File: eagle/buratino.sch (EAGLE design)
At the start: 50 parts, among them IC1 LTC3105MS, J2 AVR_SPI, J4 Ext Battery, Q2 2n7002PW, U4 ATMEGA256RFR2, U7 SWITCH, U8 LED-RGB, X1 16MHz, X2 32.768k, Y1 ANTENNA2SMD5

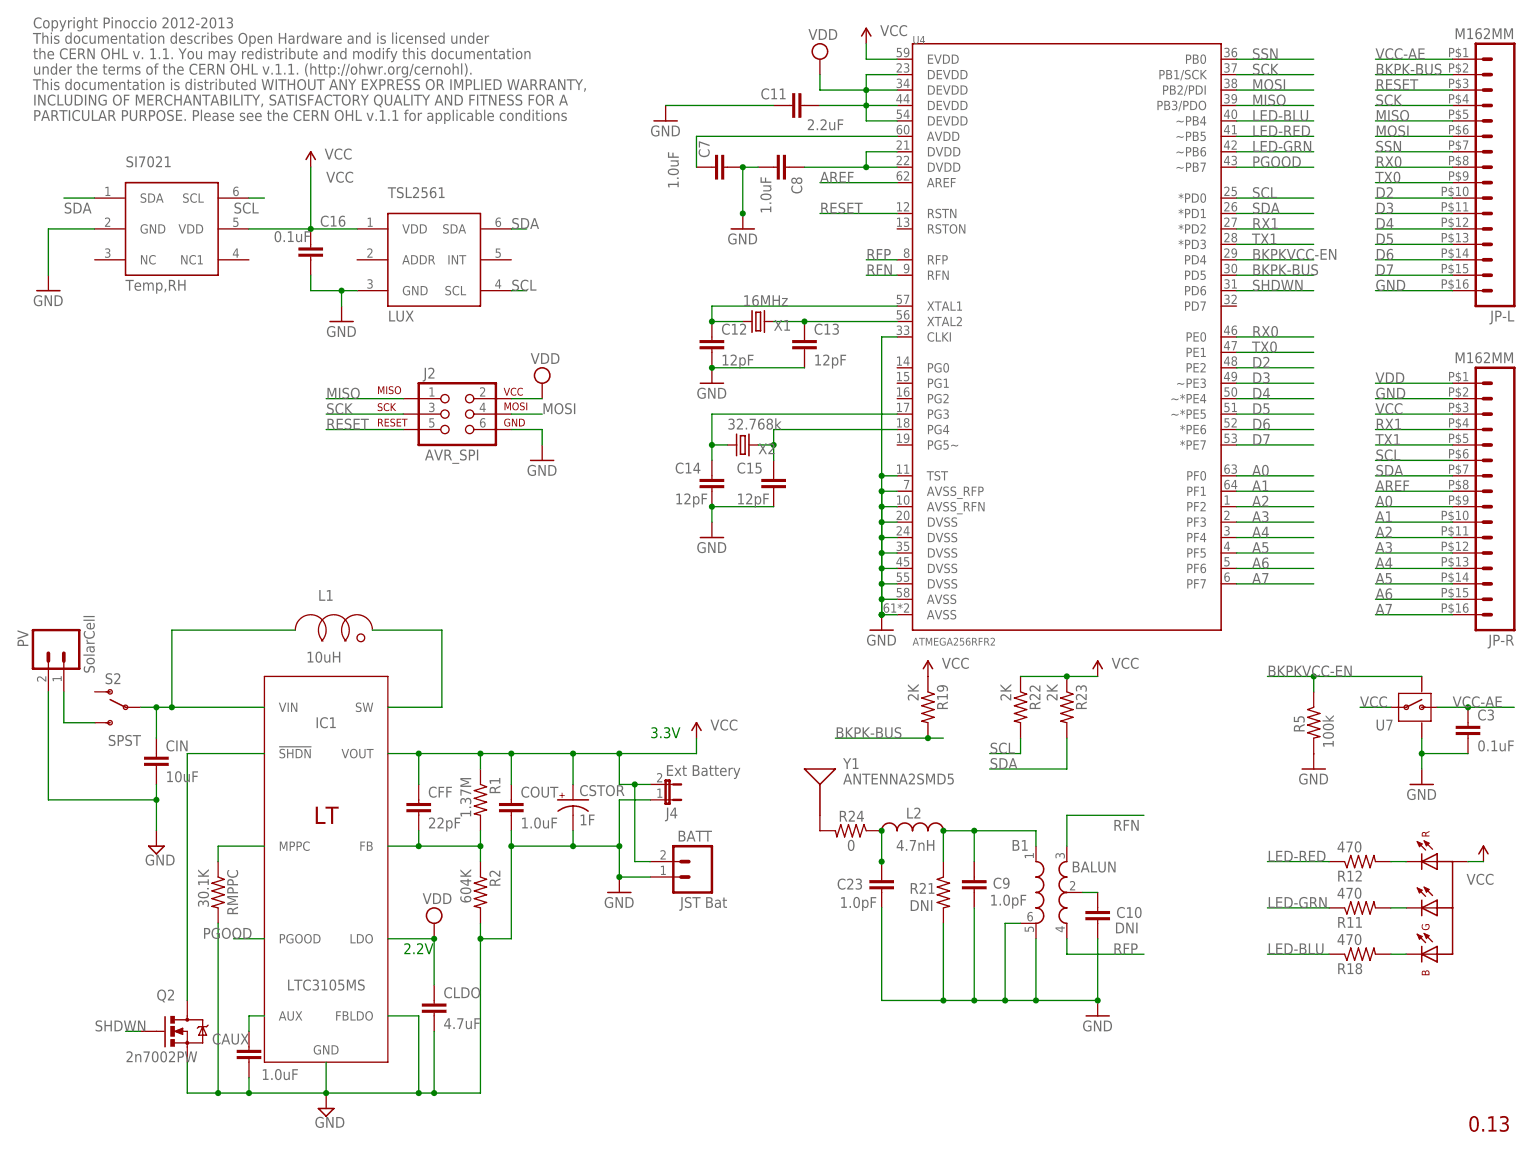
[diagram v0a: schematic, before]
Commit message: replace ICSP with JTAG
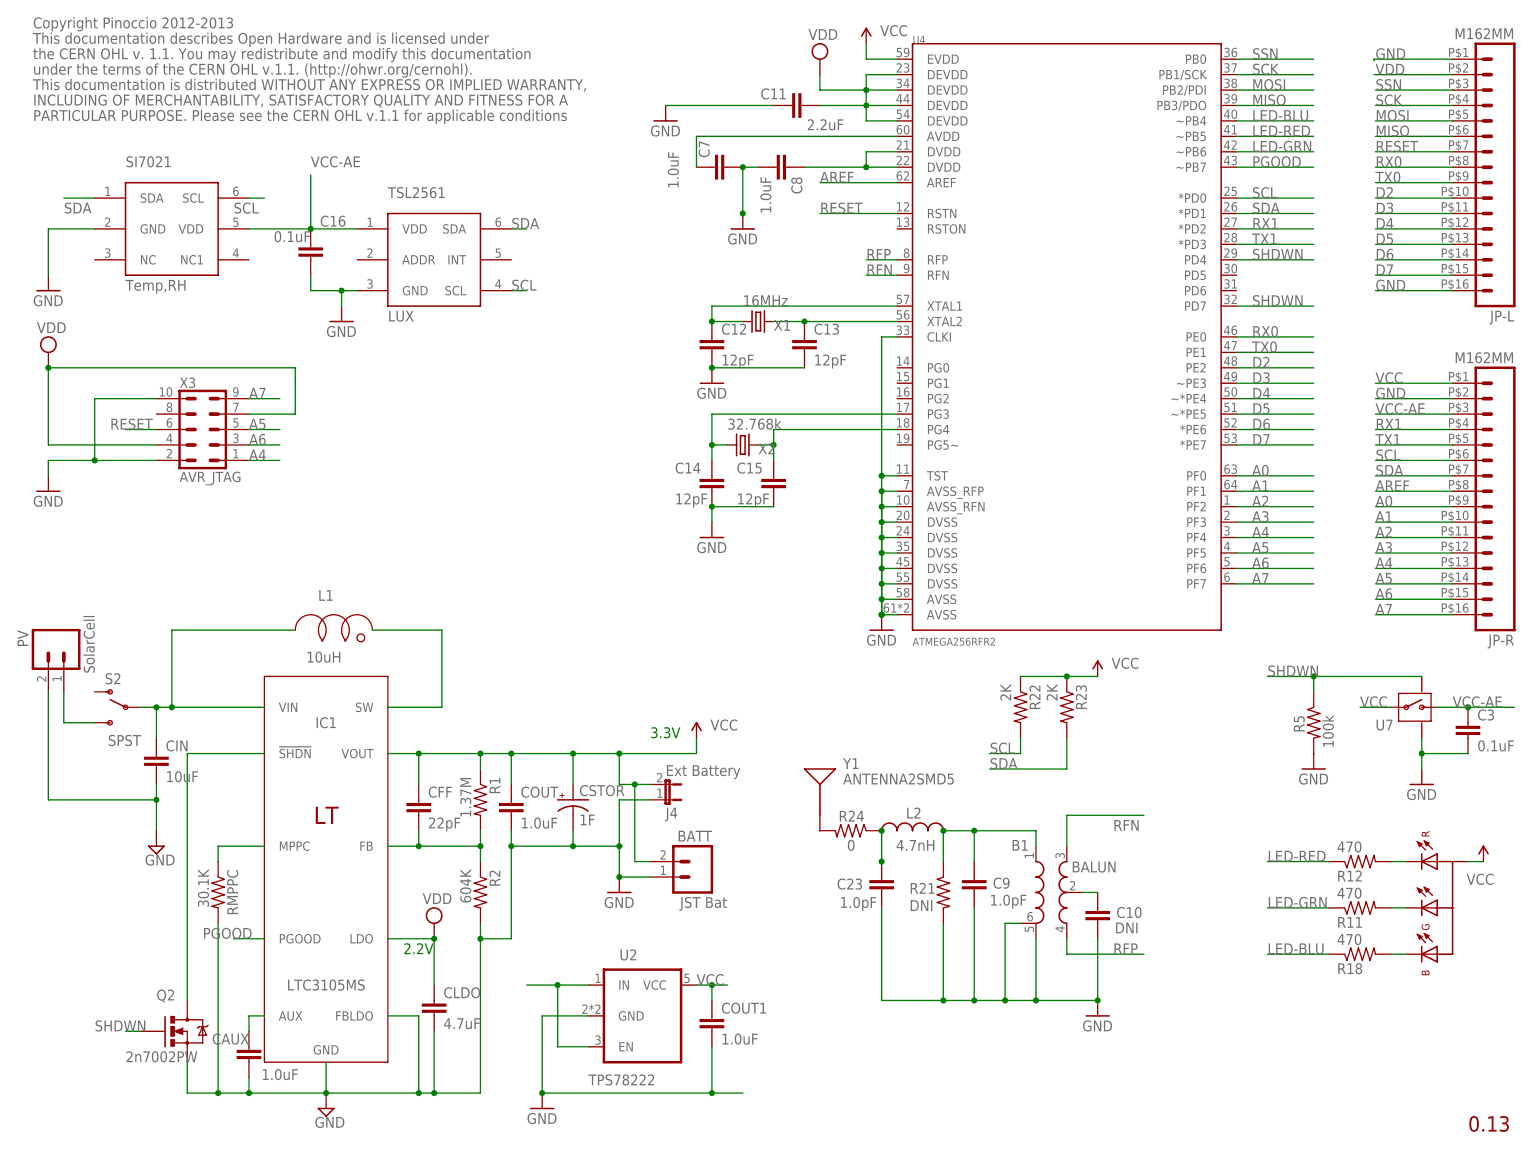
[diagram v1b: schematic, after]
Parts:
- removed J2: AVR_SPI, Pinoccio:AVR_SPI_PRG_6
- removed R19: 2K, Pinoccio:RESISTOR0402-RES
- added COUT1: 1.0uF, Pinoccio:CAP0603-CAP
- added U2: TPS78222, Pinoccio:LDO-TPS78233
- added X3: AVR_JTAG, 620-Misc:PHB_1MM27_2X05_SNS
- R22, R23: device Pinoccio:RESISTOR0603-RES -> Pinoccio:RESISTOR0402-RES
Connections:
- removed net BKPK-BUS: JP-L.2, R19.2, U4.PD5
- removed net BKPKVCC-EN: R5.1, U4.PD4, U7.ON
- new net N$66: U2.EN, U2.IN
- net A4: now also X3.1
- net A5: now also X3.5
- net A6: now also X3.3
- net A7: now also X3.9
- net GND: now also COUT1.2, JP-L.1, U2.GND, X3.10, X3.2; no longer J2.6
- net MISO: now also JP-L.6; no longer J2.1, JP-L.5
- net MOSI: now also JP-L.5; no longer J2.4, JP-L.6
- net RESET: now also JP-L.7, X3.6; no longer J2.5, JP-L.3
- net SCK: no longer J2.3
- net SHDWN: now also R5.1, U4.PD4, U4.PD7, U7.ON; no longer U4.PD6
- net SSN: now also JP-L.3; no longer JP-L.7
- net VCC: now also COUT1.1, JP-R.1, U2.VCC; no longer C16.1, JP-R.3, R19.1, SI7021.VDD, TSL2561.VDD
- net VCC-AE: now also C16.1, JP-R.3, SI7021.VDD, TSL2561.VDD; no longer JP-L.1
- net VDD: now also JP-L.2, X3.4, X3.7; no longer J2.2, JP-R.1

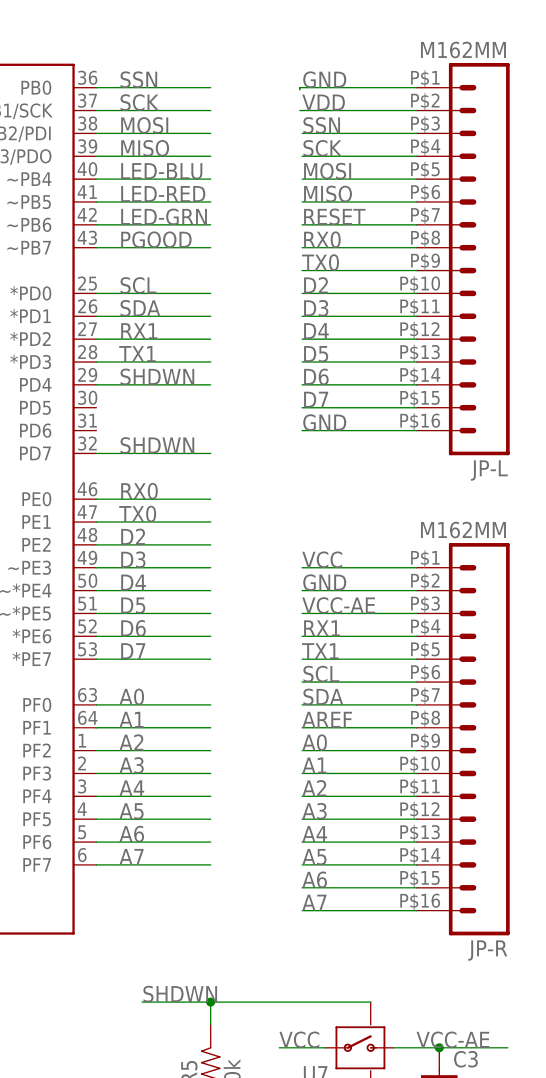
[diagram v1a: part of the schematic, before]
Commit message: replace 2mm headers with 0.1" headers
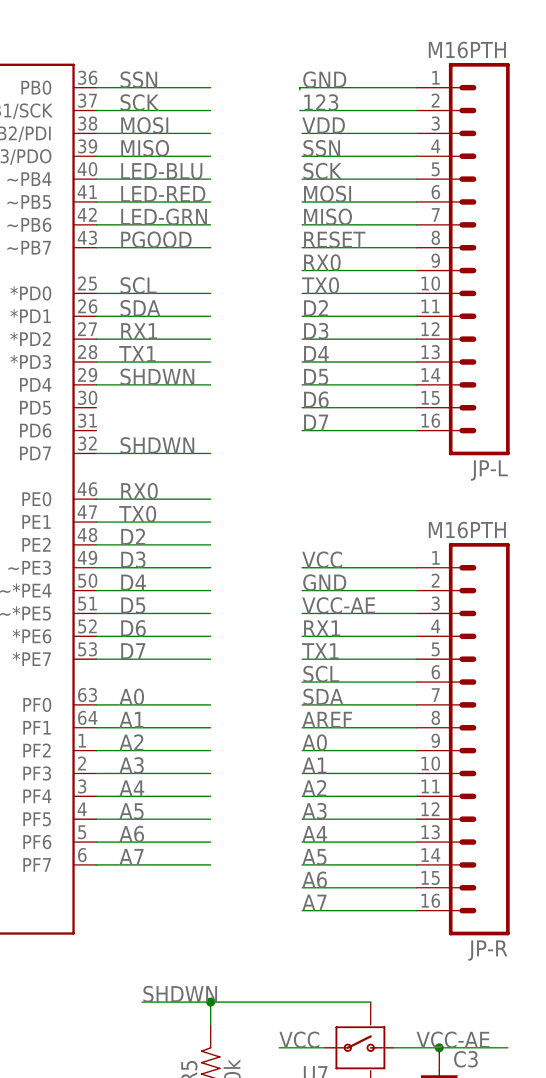
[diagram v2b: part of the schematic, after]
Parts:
- JP-L, JP-R: value M162MM -> M16PTH; device Pinoccio:M162MM -> 620-Misc:M16PTH
- R5: device Pinoccio:RESISTOR0402-RES -> Pinoccio:RESISTOR0603-RES
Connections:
- new net 123: JP-L.2
- net D2: now also JP-L.11; no longer JP-L.10
- net D3: now also JP-L.12; no longer JP-L.11
- net D4: now also JP-L.13; no longer JP-L.12
- net D5: now also JP-L.14; no longer JP-L.13
- net D6: now also JP-L.15; no longer JP-L.14
- net D7: now also JP-L.16; no longer JP-L.15
- net GND: no longer JP-L.16
- net MISO: now also JP-L.7; no longer JP-L.6
- net MOSI: now also JP-L.6; no longer JP-L.5
- net RESET: now also JP-L.8; no longer JP-L.7
- net RX0: now also JP-L.9; no longer JP-L.8
- net SCK: now also JP-L.5; no longer JP-L.4
- net SSN: now also JP-L.4; no longer JP-L.3
- net TX0: now also JP-L.10; no longer JP-L.9
- net VDD: now also JP-L.3; no longer JP-L.2
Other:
- moved on the sheet: JP-L, JP-R
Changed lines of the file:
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@@
 <part name="GND25" library="SparkFun" deviceset="GND" device=""/>
 <part name="GND28" library="SparkFun" deviceset="GND" device=""/>
-<part name="JP-R" library="Pinoccio" deviceset="M16" device="2MM"/>
-<part name="JP-L" library="Pinoccio" deviceset="M16" device="2MM"/>
+<part name="JP-R" library="620-Misc" deviceset="M16" device="PTH" value="M16PTH"/>
+<part name="JP-L" library="620-Misc" deviceset="M16" device="PTH" value="M16PTH"/>
 <part name="BATT" library="bean" deviceset="M02" device="JST-SFH" value="JST Bat"/>
 <part name="GND2" library="supply1" deviceset="GND" device=""/>
@@
 <part name="R24" library="Pinoccio" deviceset="RESISTOR" device="0402-RES" value="0"/>
 <part name="U7" library="Pinoccio" deviceset="SWITCH-MOSFET" device="TDFN4" value="SWITCH"/>
-<part name="R5" library="Pinoccio" deviceset="RESISTOR" device="0402-RES" value="100k"/>
+<part name="R5" library="Pinoccio" deviceset="RESISTOR" device="0603-RES" value="100k"/>
 <part name="GND19" library="SparkFun" deviceset="GND" device=""/>
 <part name="GND23" library="SparkFun" deviceset="GND" device=""/>
@@
 </segment>
 <segment>
-<pinref part="JP-L" gate="G$1" pin="16"/>
-<wire x1="236.22" y1="139.7" x2="223.52" y2="139.7" width="0.1524" layer="91"/>
-<label x="223.52" y="139.7" size="1.778" layer="95"/>
-</segment>
-<segment>
 <pinref part="U2" gate="G$1" pin="GND"/>
 <wire x1="93.98" y1="20.32" x2="86.36" y2="20.32" width="0.1524" layer="91"/>
@@
 </segment>
 <segment>
-<pinref part="JP-L" gate="G$1" pin="5"/>
-<wire x1="236.22" y1="167.64" x2="223.52" y2="167.64" width="0.1524" layer="91"/>
-<label x="223.52" y="167.64" size="1.778" layer="95"/>
+<pinref part="JP-L" gate="G$1" pin="6"/>
+<wire x1="236.22" y1="165.1" x2="223.52" y2="165.1" width="0.1524" layer="91"/>
+<label x="223.52" y="165.1" size="1.778" layer="95"/>
 </segment>
 </net>
@@
 </segment>
 <segment>
-<pinref part="JP-L" gate="G$1" pin="4"/>
-<wire x1="236.22" y1="170.18" x2="223.52" y2="170.18" width="0.1524" layer="91"/>
-<label x="223.52" y="170.18" size="1.778" layer="95"/>
+<pinref part="JP-L" gate="G$1" pin="5"/>
+<wire x1="236.22" y1="167.64" x2="223.52" y2="167.64" width="0.1524" layer="91"/>
+<label x="223.52" y="167.64" size="1.778" layer="95"/>
 </segment>
 </net>
@@
 </segment>
 <segment>
-<pinref part="JP-L" gate="G$1" pin="6"/>
-<wire x1="236.22" y1="165.1" x2="223.52" y2="165.1" width="0.1524" layer="91"/>
-<label x="223.52" y="165.1" size="1.778" layer="95"/>
+<pinref part="JP-L" gate="G$1" pin="7"/>
+<wire x1="236.22" y1="162.56" x2="223.52" y2="162.56" width="0.1524" layer="91"/>
+<label x="223.52" y="162.56" size="1.778" layer="95"/>
 </segment>
 </net>
@@
 <net name="D2" class="0">
 <segment>
-<pinref part="JP-L" gate="G$1" pin="10"/>
-<wire x1="236.22" y1="154.94" x2="223.52" y2="154.94" width="0.1524" layer="91"/>
-<label x="223.52" y="154.94" size="1.778" layer="95"/>
-</segment>
-<segment>
 <pinref part="U4" gate="G$1" pin="PE2"/>
 <wire x1="200.66" y1="127" x2="213.36" y2="127" width="0.1524" layer="91"/>
 <label x="203.2" y="127" size="1.778" layer="95"/>
 </segment>
-</net>
-<net name="D3" class="0">
 <segment>
 <pinref part="JP-L" gate="G$1" pin="11"/>
@@
 <label x="223.52" y="152.4" size="1.778" layer="95"/>
 </segment>
+</net>
+<net name="D3" class="0">
 <segment>
 <pinref part="U4" gate="G$1" pin="~PE3"/>
@@
 <label x="203.2" y="124.46" size="1.778" layer="95"/>
 </segment>
-</net>
-<net name="D4" class="0">
 <segment>
 <pinref part="JP-L" gate="G$1" pin="12"/>
@@
 <label x="223.52" y="149.86" size="1.778" layer="95"/>
 </segment>
+</net>
+<net name="D4" class="0">
 <segment>
 <pinref part="U4" gate="G$1" pin="~*PE4"/>
@@
 <label x="203.2" y="121.92" size="1.778" layer="95"/>
 </segment>
-</net>
-<net name="D5" class="0">
 <segment>
 <pinref part="JP-L" gate="G$1" pin="13"/>
@@
 <label x="223.52" y="147.32" size="1.778" layer="95"/>
 </segment>
+</net>
+<net name="D5" class="0">
 <segment>
 <pinref part="U4" gate="G$1" pin="~*PE5"/>
@@
 <label x="203.2" y="119.38" size="1.778" layer="95"/>
 </segment>
-</net>
-<net name="D6" class="0">
 <segment>
 <pinref part="JP-L" gate="G$1" pin="14"/>
@@
 <label x="223.52" y="144.78" size="1.778" layer="95"/>
 </segment>
+</net>
+<net name="D6" class="0">
 <segment>
 <pinref part="U4" gate="G$1" pin="*PE6"/>
@@
 <label x="203.2" y="116.84" size="1.778" layer="95"/>
 </segment>
-</net>
-<net name="D7" class="0">
 <segment>
 <pinref part="JP-L" gate="G$1" pin="15"/>
@@
 <label x="223.52" y="142.24" size="1.778" layer="95"/>
 </segment>
+</net>
+<net name="D7" class="0">
 <segment>
 <pinref part="U4" gate="G$1" pin="*PE7"/>
@@
 <label x="203.2" y="114.3" size="1.778" layer="95"/>
 </segment>
+<segment>
+<pinref part="JP-L" gate="G$1" pin="16"/>
+<wire x1="236.22" y1="139.7" x2="223.52" y2="139.7" width="0.1524" layer="91"/>
+<label x="223.52" y="139.7" size="1.778" layer="95"/>
+</segment>
 </net>
 <net name="AREF" class="0">
@@
 </segment>
 <segment>
-<pinref part="JP-L" gate="G$1" pin="3"/>
-<wire x1="236.22" y1="172.72" x2="223.52" y2="172.72" width="0.1524" layer="91"/>
-<label x="223.52" y="172.72" size="1.778" layer="95"/>
+<pinref part="JP-L" gate="G$1" pin="4"/>
+<wire x1="236.22" y1="170.18" x2="223.52" y2="170.18" width="0.1524" layer="91"/>
+<label x="223.52" y="170.18" size="1.778" layer="95"/>
 </segment>
 </net>
@@
 </segment>
 <segment>
-<pinref part="JP-L" gate="G$1" pin="8"/>
-<wire x1="236.22" y1="160.02" x2="223.52" y2="160.02" width="0.1524" layer="91"/>
-<label x="223.52" y="160.02" size="1.778" layer="95"/>
+<pinref part="JP-L" gate="G$1" pin="9"/>
+<wire x1="236.22" y1="157.48" x2="223.52" y2="157.48" width="0.1524" layer="91"/>
+<label x="223.52" y="157.48" size="1.778" layer="95"/>
 </segment>
 </net>
@@
 </segment>
 <segment>
-<pinref part="JP-L" gate="G$1" pin="9"/>
-<wire x1="236.22" y1="157.48" x2="223.52" y2="157.48" width="0.1524" layer="91"/>
-<label x="223.52" y="157.48" size="1.778" layer="95"/>
+<pinref part="JP-L" gate="G$1" pin="10"/>
+<wire x1="236.22" y1="154.94" x2="223.52" y2="154.94" width="0.1524" layer="91"/>
+<label x="223.52" y="154.94" size="1.778" layer="95"/>
 </segment>
 </net>
@@
 </segment>
 <segment>
-<pinref part="JP-L" gate="G$1" pin="7"/>
-<wire x1="236.22" y1="162.56" x2="223.52" y2="162.56" width="0.1524" layer="91"/>
-<label x="223.52" y="162.56" size="1.778" layer="95"/>
+<pinref part="JP-L" gate="G$1" pin="8"/>
+<wire x1="236.22" y1="160.02" x2="223.52" y2="160.02" width="0.1524" layer="91"/>
+<label x="223.52" y="160.02" size="1.778" layer="95"/>
 </segment>
 </net>
@@
 </segment>
 <segment>
-<pinref part="JP-L" gate="G$1" pin="2"/>
-<wire x1="236.22" y1="175.26" x2="223.266" y2="175.26" width="0.1524" layer="91"/>
-<label x="223.52" y="175.26" size="1.778" layer="95"/>
+<pinref part="JP-L" gate="G$1" pin="3"/>
+<wire x1="236.22" y1="172.72" x2="223.52" y2="172.72" width="0.1524" layer="91"/>
+<label x="223.52" y="172.72" size="1.778" layer="95"/>
 </segment>
 </net>
@@
 </segment>
 </net>
+<net name="123" class="0">
+<segment>
+<pinref part="JP-L" gate="G$1" pin="2"/>
+<wire x1="236.22" y1="175.26" x2="223.266" y2="175.26" width="0.1524" layer="91"/>
+<label x="223.52" y="175.26" size="1.778" layer="95"/>
+</segment>
+</net>

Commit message: add PIR
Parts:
- added J1: Vcc-Vdd Tie, Pinoccio:SOLDERJUMPERNO
- added J2: Ext Battery, Pinoccio:JUMPER-2PTH
- added R3: 10K, Pinoccio:RESISTOR0603-RES
- added R4: 47K, Pinoccio:RESISTOR0603-RES
- added S1: (no value), SparkFun-Electromechanical:TAC_SWITCHPTH
- added U$1: IRS-B210ST01R1, 620-Sensors:IRS-B210ST01R1
- BATT: value JST Bat -> Aux Bat
- J4: value Ext Battery -> Aux Batt
- R11, R12, R18, R22, R23: device Pinoccio:RESISTOR0402-RES -> Pinoccio:RESISTOR0603-RES
- VIN1: value SolarCell -> Ext Power
- renumbered PV to VIN1
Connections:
- removed net 123: JP-L.2
- removed net N$66: U2.EN, U2.IN
- removed net N$9: CIN.1, IC1.VIN, L1.A, S2.P
- new net BTN: R3.2, S1.3, S1.4, U4.PD7
- new net VIN: CIN.1, IC1.VIN, L1.A, S2.P, U2.EN, U2.IN
- net A0: now also R4.1, U$1.S
- net GND: now also J2.1, R4.2, S1.1, S1.2, U$1.GND
- net N$24: now also J2.2
- net SHDWN: now also U4.PD6; no longer U4.PD4, U4.PD7
- net VCC: now also J1.1, JP-L.3
- net VDD: now also J1.2, JP-L.2, R3.1, U$1.VIN; no longer JP-L.3
